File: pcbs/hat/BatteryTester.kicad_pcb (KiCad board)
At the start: 2 copper layers, 49 parts, among them Q1 Q_NMOS_DGS, Q10 Q_NMOS_DGS, Q11 Q_NMOS_DGS, Q12 Q_NMOS_DGS, Q13 Q_NMOS_DGS, Q14 Q_NMOS_DGS, Q15 Q_NMOS_DGS, Q16 Q_NMOS_DGS, Q2 Q_NMOS_DGS, Q3 Q_NMOS_DGS, Q4 Q_NMOS_DGS, Q5 Q_NMOS_DGS, Q6 Q_NMOS_DGS, Q7 Q_NMOS_DGS, Q8 Q_NMOS_DGS, Q9 Q_NMOS_DGS, U1 NUCLEO-F401RE, U10 INA195, U12 INA195, U14 INA195, U16 INA195, U2 INA195, U4 INA195, U6 INA195, U8 INA195

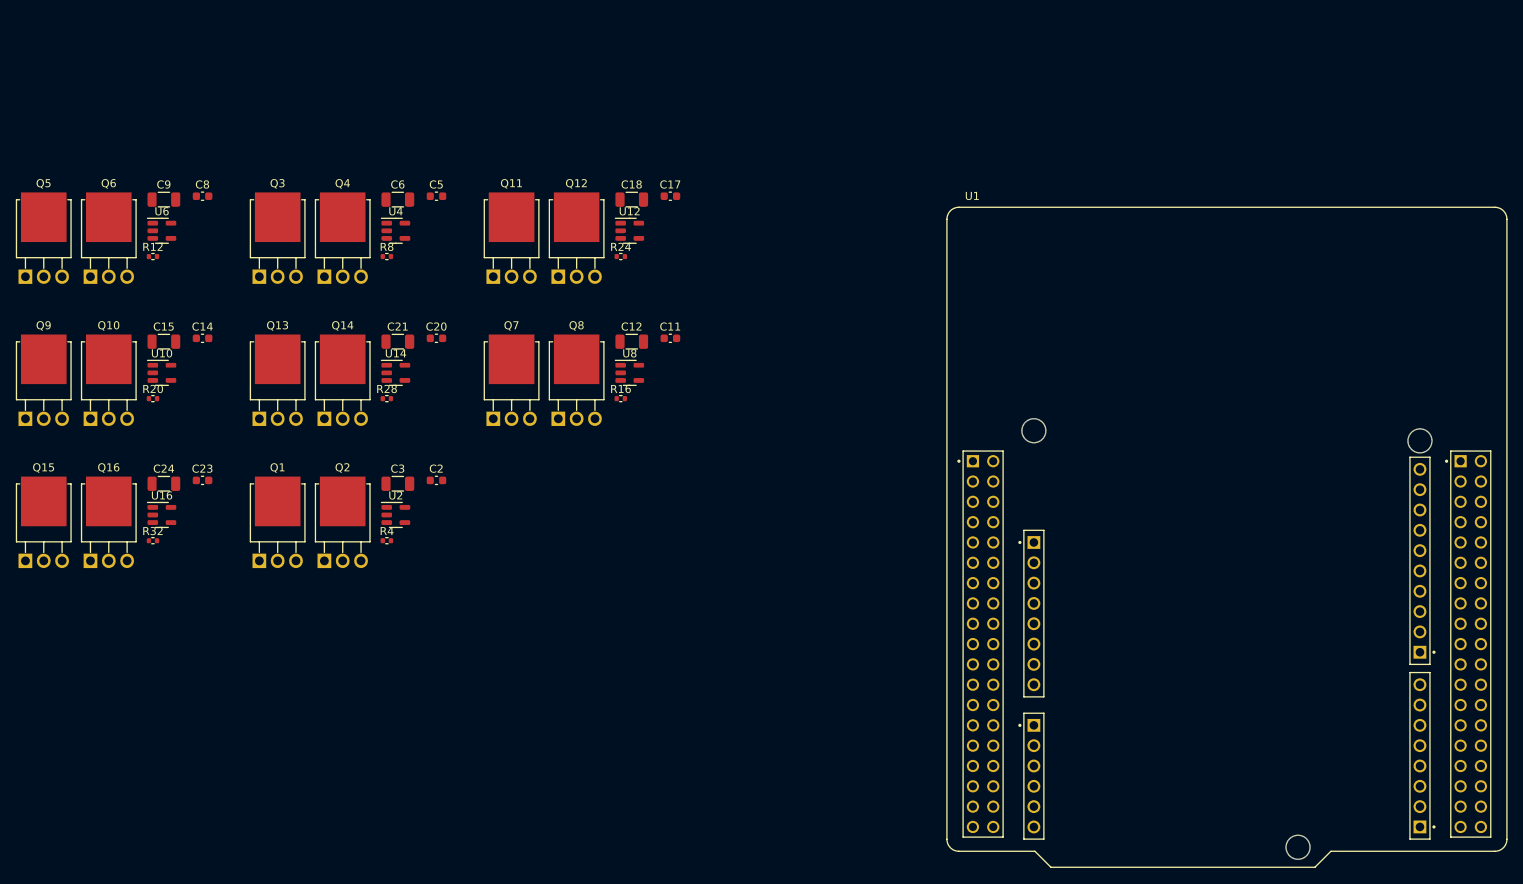
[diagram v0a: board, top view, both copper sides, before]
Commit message: fix symbol and footprint libraries
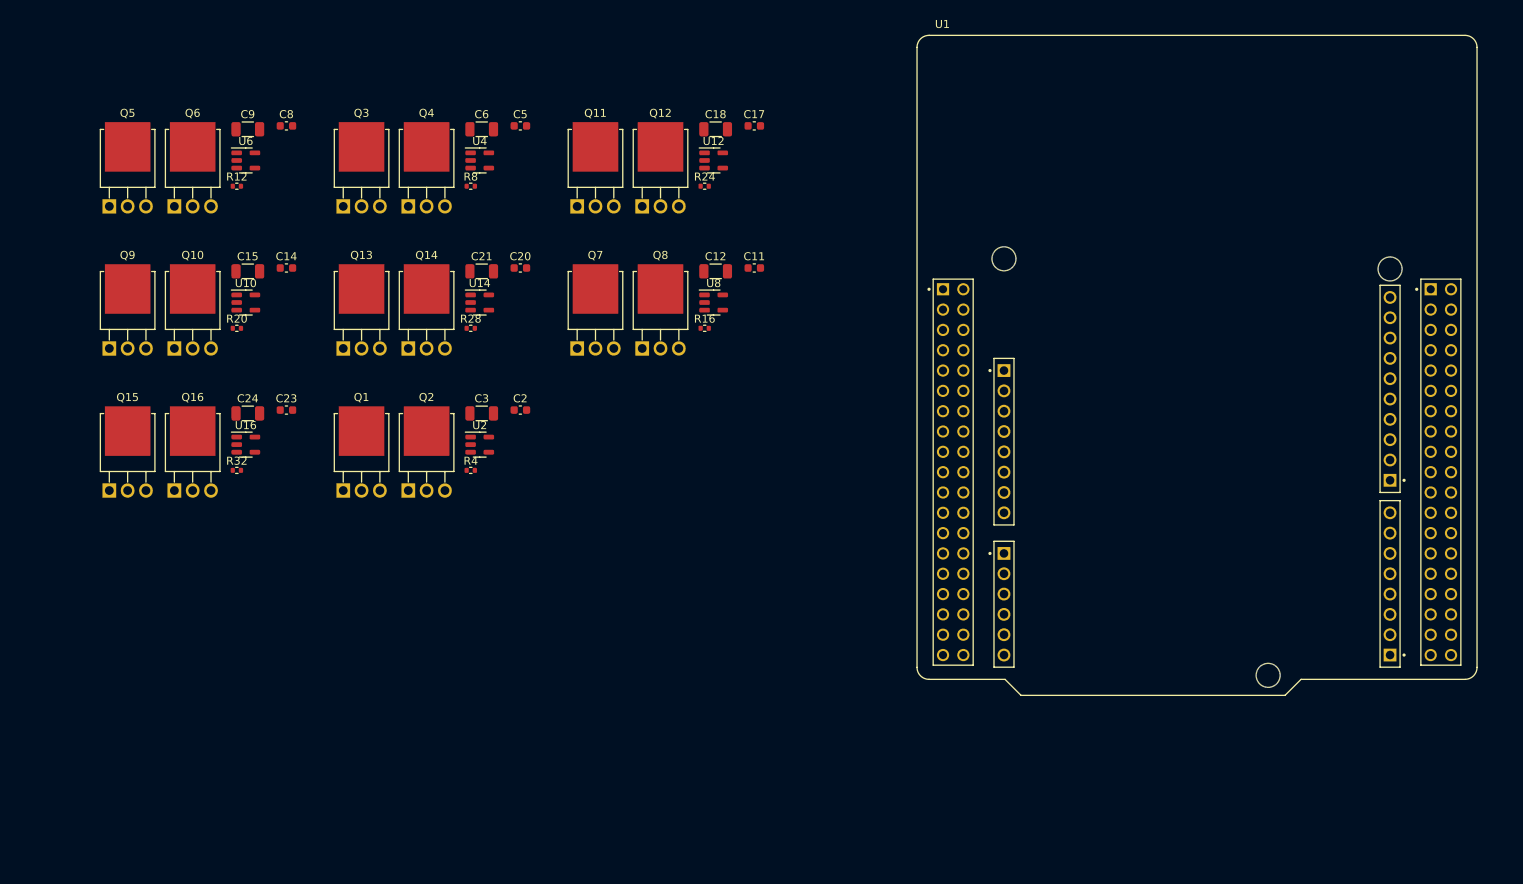
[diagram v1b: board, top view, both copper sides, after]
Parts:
- U1: footprint STS_Boards:ST_NUCLEO-F401RE -> STS_Boards:ST_Morpho_Connector_64_MountingHoles
- moved U1 21.8 mm to (164.7, 64.4)
- moved Q14 13.7 mm to (66.1, 62.2)
- moved Q7 13.7 mm to (87.2, 62.2)
- moved Q8 13.7 mm to (95.3, 62.2)
- moved R32 13.7 mm to (44.6, 77.5)
- moved R4 13.7 mm to (73.9, 77.5)
- moved Q10 13.7 mm to (36.8, 62.2)
- moved Q9 13.7 mm to (28.7, 62.2)
- moved C11 13.7 mm to (109.3, 52.2)
- moved C12 13.7 mm to (104.5, 52.6)
- moved C17 13.7 mm to (109.3, 34.4)
- moved C18 13.7 mm to (104.5, 34.9)
- moved Q11 13.7 mm to (87.2, 44.5)
- moved Q12 13.7 mm to (95.3, 44.5)
- moved Q13 13.7 mm to (57.9, 62.2)
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
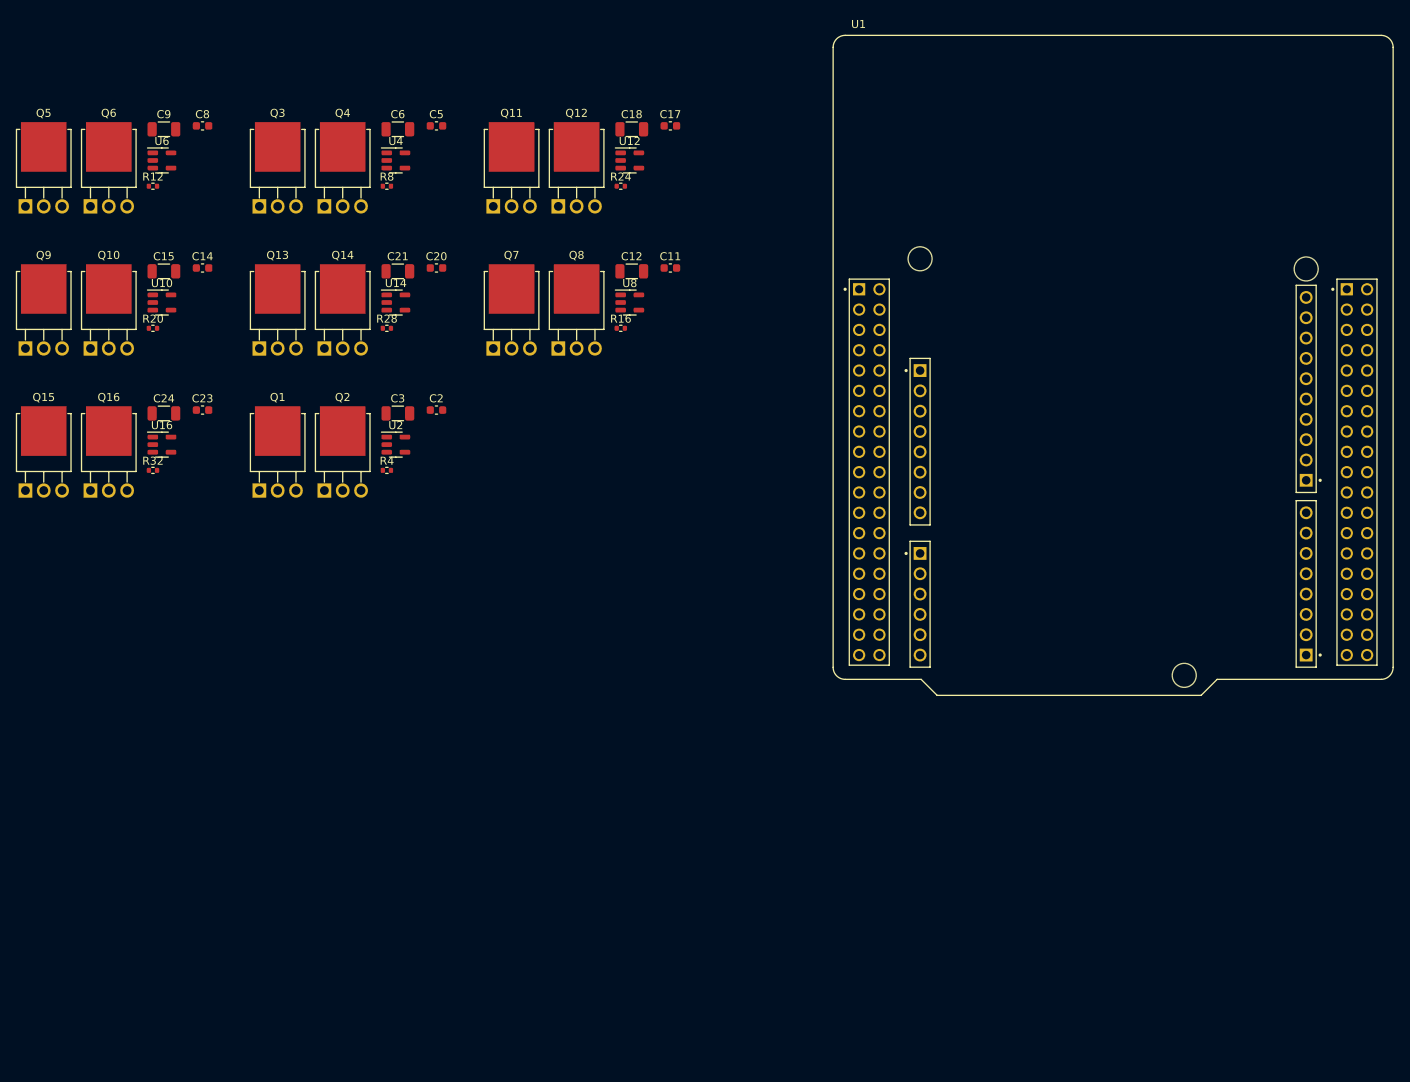
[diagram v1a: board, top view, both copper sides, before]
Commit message: add ADCs
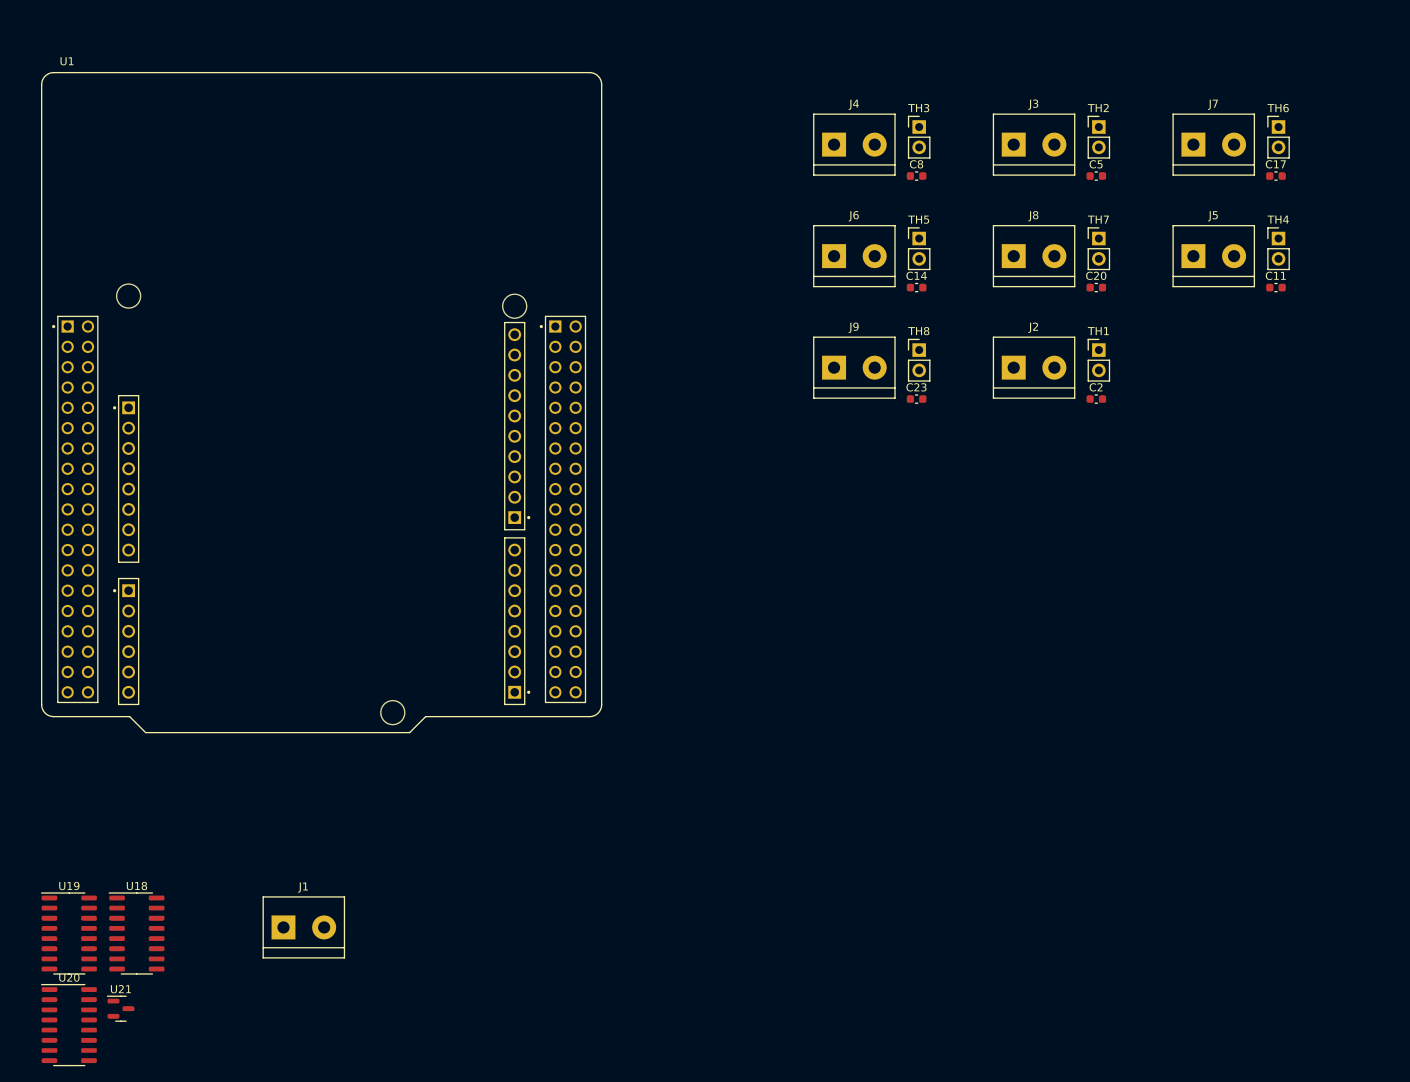
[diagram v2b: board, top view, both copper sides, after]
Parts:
- removed C12, C15, C18, C21, C24, C3, C6, C9: 1µ, Capacitor_SMD:C_1206_3216Metric
- removed Q1, Q10, Q11, Q12, Q13, Q14, Q15, Q16, Q2, Q3, Q4, Q5, Q6, Q7, Q8, Q9: Q_NMOS_DGS, Package_TO_SOT_THT:TO-251-3-1EP_Horizontal_TabDown
- removed R12, R16, R20, R24, R28, R32, R4, R8: 10k, Resistor_SMD:R_0402_1005Metric
- removed U10, U12, U14, U16, U2, U4, U6, U8: INA195, Package_TO_SOT_SMD:SOT-23-5
- added J1: Screw_Terminal_01x02, TerminalBlock:TerminalBlock_bornier-2_P5.08mm, F.Cu at (61.0, 134.6)
- added J2: Conn_01x02_Female, TerminalBlock:TerminalBlock_bornier-2_P5.08mm, F.Cu at (152.2, 64.7)
- added J3: Conn_01x02_Female, TerminalBlock:TerminalBlock_bornier-2_P5.08mm, F.Cu at (152.2, 36.8)
- added J4: Conn_01x02_Female, TerminalBlock:TerminalBlock_bornier-2_P5.08mm, F.Cu at (129.8, 36.8)
- added J5: Conn_01x02_Female, TerminalBlock:TerminalBlock_bornier-2_P5.08mm, F.Cu at (174.7, 50.7)
- added J6: Conn_01x02_Female, TerminalBlock:TerminalBlock_bornier-2_P5.08mm, F.Cu at (129.8, 50.7)
- added J7: Conn_01x02_Female, TerminalBlock:TerminalBlock_bornier-2_P5.08mm, F.Cu at (174.7, 36.8)
- added J8: Conn_01x02_Female, TerminalBlock:TerminalBlock_bornier-2_P5.08mm, F.Cu at (152.2, 50.7)
- added J9: Conn_01x02_Female, TerminalBlock:TerminalBlock_bornier-2_P5.08mm, F.Cu at (129.8, 64.7)
- added TH1: Thermistor_NTC, Connector_PinHeader_2.54mm:PinHeader_1x02_P2.54mm_Vertical, F.Cu at (162.9, 62.5)
- added TH2: Thermistor_NTC, Connector_PinHeader_2.54mm:PinHeader_1x02_P2.54mm_Vertical, F.Cu at (162.9, 34.6)
- added TH3: Thermistor_NTC, Connector_PinHeader_2.54mm:PinHeader_1x02_P2.54mm_Vertical, F.Cu at (140.4, 34.6)
- added TH4: Thermistor_NTC, Connector_PinHeader_2.54mm:PinHeader_1x02_P2.54mm_Vertical, F.Cu at (185.3, 48.5)
- added TH5: Thermistor_NTC, Connector_PinHeader_2.54mm:PinHeader_1x02_P2.54mm_Vertical, F.Cu at (140.4, 48.5)
- added TH6: Thermistor_NTC, Connector_PinHeader_2.54mm:PinHeader_1x02_P2.54mm_Vertical, F.Cu at (185.3, 34.6)
- added TH7: Thermistor_NTC, Connector_PinHeader_2.54mm:PinHeader_1x02_P2.54mm_Vertical, F.Cu at (162.9, 48.5)
- added TH8: Thermistor_NTC, Connector_PinHeader_2.54mm:PinHeader_1x02_P2.54mm_Vertical, F.Cu at (140.4, 62.5)
- added U18: MCP3008, Package_SO:SOIC-16_3.9x9.9mm_P1.27mm, F.Cu at (42.6, 135.4)
- added U19: MCP3008, Package_SO:SOIC-16_3.9x9.9mm_P1.27mm, F.Cu at (34.2, 135.4)
- added U20: MCP3008, Package_SO:SOIC-16_3.9x9.9mm_P1.27mm, F.Cu at (34.2, 146.8)
- added U21: ???, Package_TO_SOT_SMD:SOT-23, F.Cu at (40.6, 144.8)
- moved U1 99.0 mm to (65.7, 69.0)
- moved C8 89.5 mm to (140.1, 40.7)
- moved C14 89.3 mm to (140.1, 54.6)
- moved C23 89.3 mm to (140.1, 68.6)
- moved C5 82.7 mm to (162.6, 40.7)
- moved C20 82.5 mm to (162.6, 54.6)
- moved C2 82.5 mm to (162.6, 68.6)
- moved C17 76.0 mm to (185.0, 40.7)
- moved C11 75.7 mm to (185.0, 54.6)
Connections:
- U1 pad CN7_16: unconnected-(U1-PadCN7_16) -> +5V
- U1 pad CN7_18: unconnected-(U1-PadCN7_18) -> +3.3V
- U1 pad CN7_19: Net-(U1-PadCN7_19) -> GND
- U1 pad CN7_20: Net-(U1-PadCN7_19) -> GND
- U1 pad CN7_22: Net-(U1-PadCN7_19) -> GND
- U1 pad CN7_24: unconnected-(U1-PadCN7_24) -> VCC
- U1 pad CN7_8: Net-(U1-PadCN7_19) -> GND
- U1 pad CN8_4: /SENSOR_12 -> unconnected-(U1-PadCN8_4)
- U1 pad CN8_5: /SENSOR_20 -> unconnected-(U1-PadCN8_5)
- U1 pad CN8_6: /SENSOR_10 -> unconnected-(U1-PadCN8_6)
